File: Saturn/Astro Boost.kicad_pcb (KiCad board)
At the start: 2 copper layers, 59 x 130 mm, 35 parts, among them J1 AudioJack2, J10 Power from SW to PS, J11 +9V, J12 -9V, J2 AudioJack2, J3 Jack-DC, J4 Signal In, J5 Audio In, J6 Processed to SW, J7 Bypass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

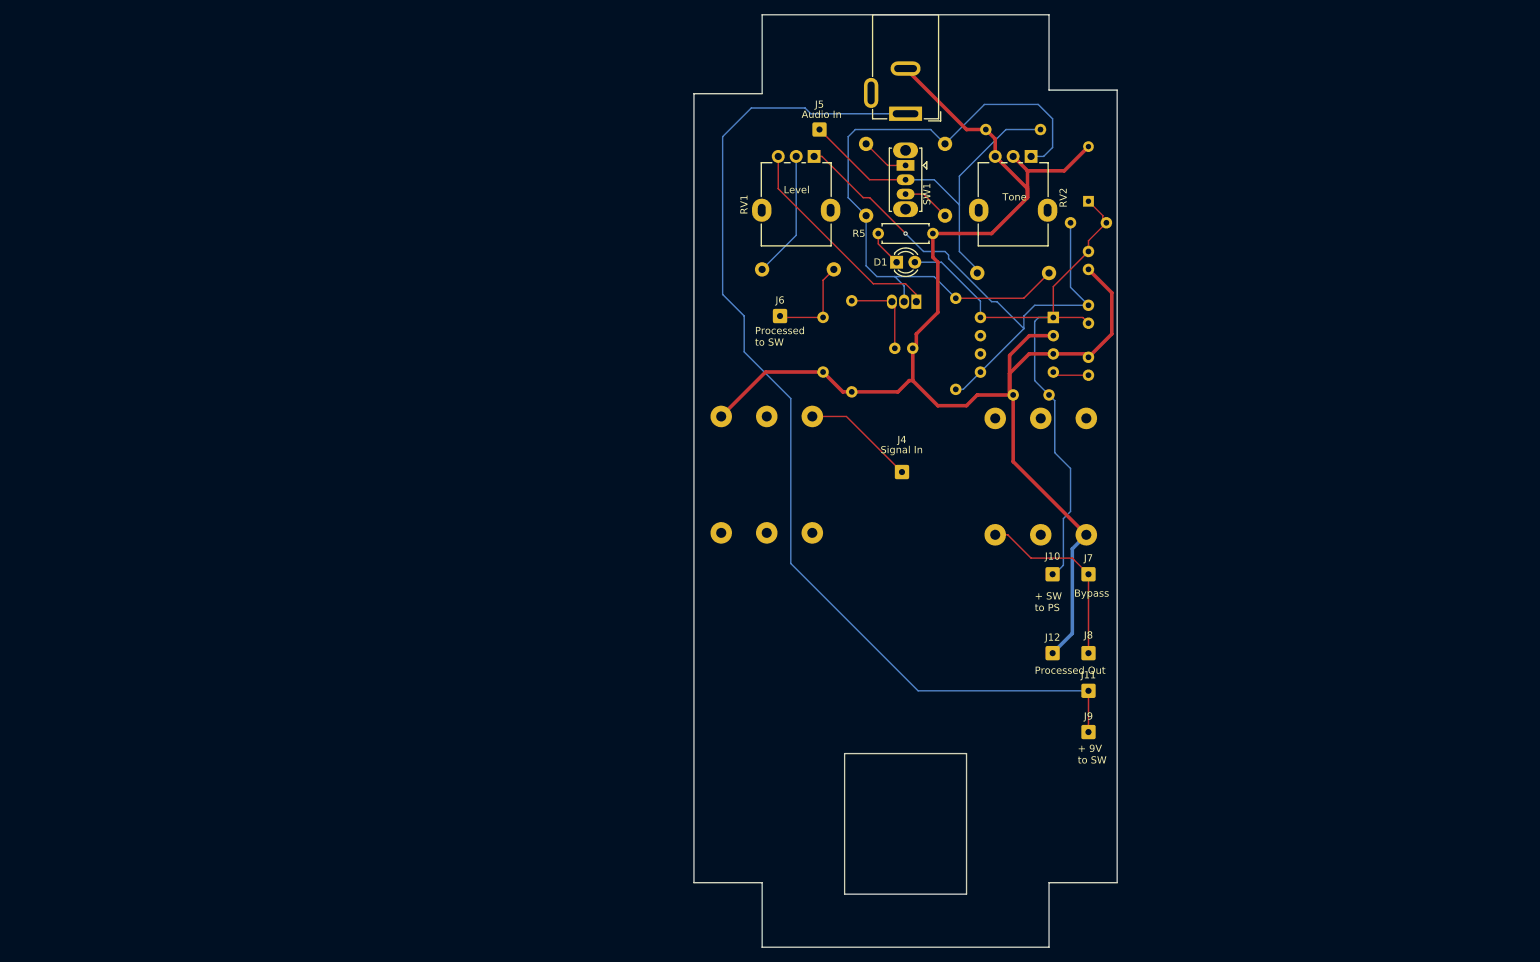
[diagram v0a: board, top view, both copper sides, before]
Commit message: Updates to Saturn
Removed wiring pads and associated tracks
Added to do list
Shortened PCB
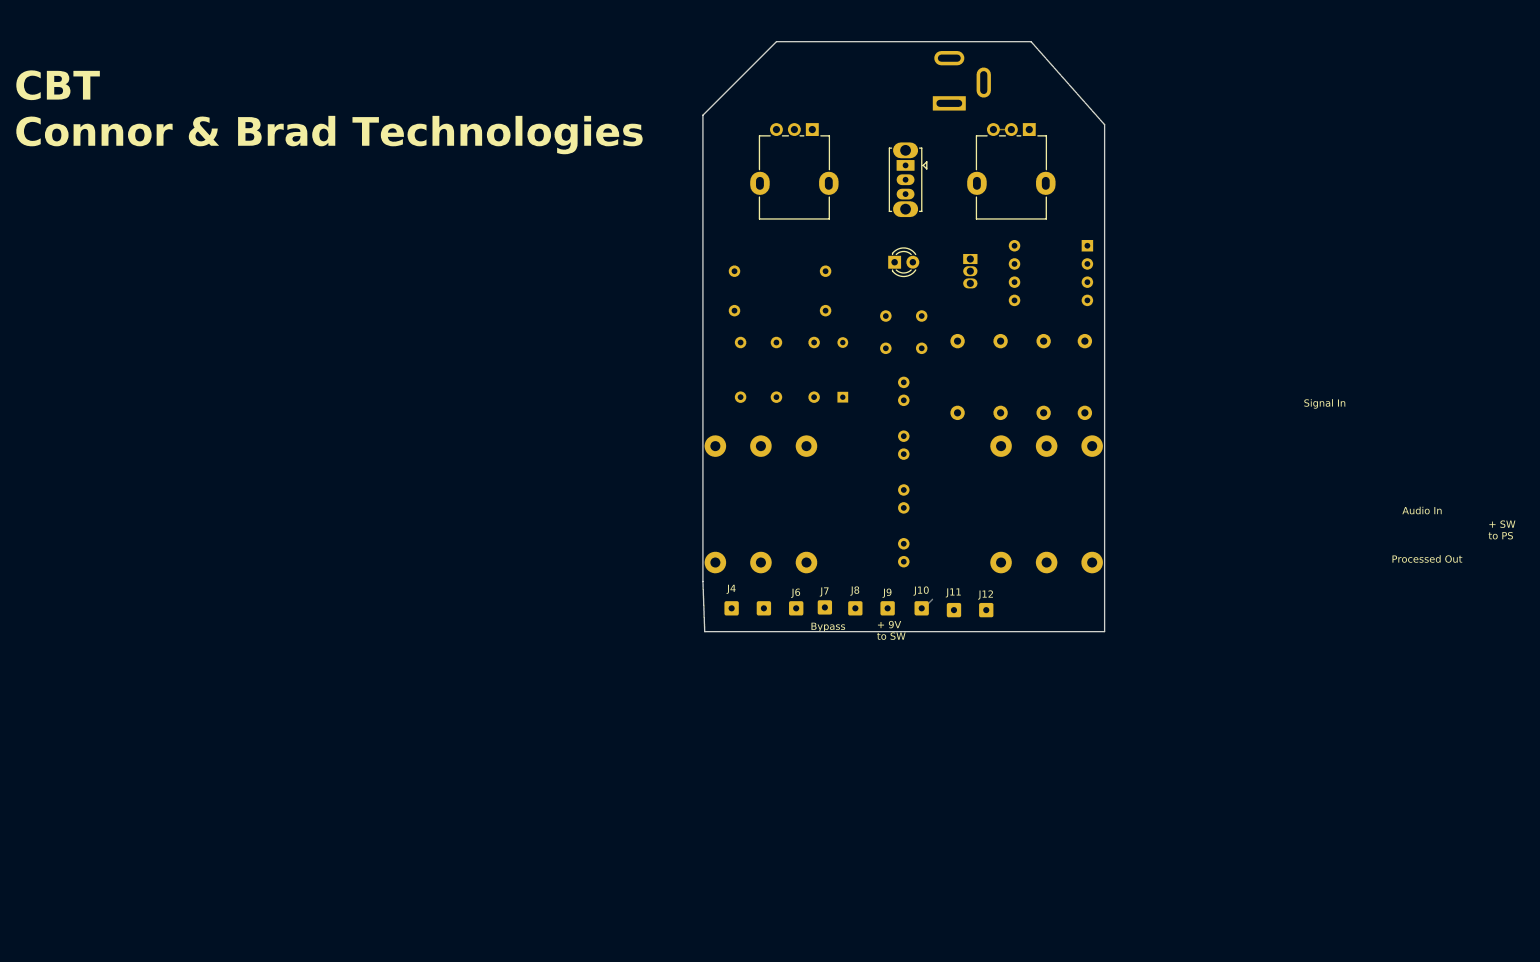
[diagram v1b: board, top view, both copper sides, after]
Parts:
- J3, R5: moved to B.Cu
- moved J5 67.2 mm to (130.8, 104.0)
- moved R4 56.0 mm to (127.5, 74.6), turned to 90 degrees
- moved D2 43.8 mm to (141.8, 74.6)
- moved C5 42.3 mm to (175.5, 76.8), turned to 90 degrees
- moved J6 40.8 mm to (135.2, 104.0)
- moved C8 38.4 mm to (150.2, 97.5), turned to 90 degrees
- moved J7 37.0 mm to (139.2, 103.9)
- moved C4 37.0 mm to (169.8, 76.8)
- moved C6 34.7 mm to (150.2, 87.5), turned to -90 degrees
- moved J8 33.1 mm to (143.5, 104.0)
- moved J9 32.9 mm to (148.0, 104.0)
- moved C9 31.6 mm to (150.2, 72.5)
- moved J4 30.4 mm to (126.2, 104.0)
- moved C7 28.8 mm to (152.8, 63.2)
- moved BT1 27.5 mm to (148.5, 121.8)
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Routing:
- net 0: track 213.2 -> 2.50 mm
- net Power from 9V: track 145.5 -> 0.00 mm
- net Net-(Q1-B): track 92.3 -> 0.00 mm
- net +9V: track 90.7 -> 2.02 mm
- net -9V: track 76.4 -> 0.00 mm, vias 1 -> 0
- net Audio In: track 52.4 -> 0.00 mm
- net Net-(Q1-C): track 30.9 -> 0.00 mm
- net Net-(J7-Pin_1): track 27.0 -> 0.75 mm
- net Net-(C2-Pad2): track 17.7 -> 0.00 mm
- net Net-(J4-Pin_1): track 15.7 -> 0.00 mm
- net Processed to SW: track 13.4 -> 0.27 mm
- net Net-(Q1-E): track 12.3 -> 0.00 mm
- net Net-(SW1-C): track 6.74 -> 0.00 mm
- net Net-(SW1-A): track 6.74 -> 0.00 mm
- net Net-(U1-CAP-): track 5.08 -> 0.00 mm
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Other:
- board size 59 x 130 mm -> 56 x 82.2 mm
- board text added: "CBT Connor & Brad Technologies"
- board text removed: "Level"
- board text removed: "Processed to SW"
- board text removed: "Tone"

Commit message: Saturn PCB Updates
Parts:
- R2, R4, R5: footprint Resistor_THT:R_Axial_DIN0207_L6.3mm_D2.5mm_P7.62mm_Horizontal -> Resistor_THT:R_Axial_DIN0207_L6.3mm_D2.5mm_P10.16mm_Horizontal
- U1: footprint Package_DIP:DIP-8_W10.16mm -> Package_DIP:DIP-8_W7.62mm
- moved D2 14.7 mm to (127.2, 72.8), turned to 0 degrees
- moved R4 12.4 mm to (126.2, 62.2), turned to 0 degrees
- moved R3 4.54 mm to (125.0, 58.2)
- moved R2 4.35 mm to (136.3, 69.0), turned to 180 degrees
- moved R1 3.35 mm to (137.8, 54.0)
- moved R5 2.02 mm to (136.3, 65.5), turned to 180 degrees
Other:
- board text added: "+ -"

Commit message: updates to saturn
layout
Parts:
- moved R4 46.1 mm to (171.2, 52.0), turned to 180 degrees
- moved C4 38.9 mm to (143.5, 48.0)
- moved C5 38.4 mm to (145.5, 52.8), turned to 0 degrees
- moved R1 34.5 mm to (172.2, 56.0)
- moved C1 28.8 mm to (157.5, 38.0)
- moved D2 28.0 mm to (154.1, 80.5), turned to 180 degrees
- moved R2 27.8 mm to (146.5, 94.8), turned to 90 degrees
- moved U1 26.6 mm to (154.1, 68.7)
- moved C8 23.7 mm to (160.2, 76.0)
- moved C3 21.1 mm to (140.5, 63.8)
- moved C2 20.9 mm to (152.8, 84.5)
- moved C6 16.5 mm to (140.8, 74.0)
- moved R3 16.3 mm to (141.2, 56.2), turned to 180 degrees
- moved C9 15.1 mm to (160.2, 61.2)
- moved C10 15.0 mm to (162.8, 68.5), turned to 180 degrees
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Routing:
- net 0: track 2.50 -> 0.00 mm
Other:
- outline, holes or cut-outs redrawn
- board text added: "+"
- board text removed: "+ 9V to SW"
- board text removed: "+ SW to PS"
- board text removed: "Audio In"
- board text removed: "Bypass"
- board text removed: "Processed Out"
- board text removed: "Signal In"

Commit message: Updates to saturn
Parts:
- C1, C5: footprint Capacitor_THT:C_Disc_D9.0mm_W5.0mm_P10.00mm -> Capacitor_THT:C_Axial_L12.0mm_D6.5mm_P20.00mm_Horizontal
- C2, C4: footprint Capacitor_THT:C_Disc_D9.0mm_W5.0mm_P10.00mm -> Capacitor_THT:C_Axial_L12.0mm_D9.5mm_P20.00mm_Horizontal
- J10, J11, J12, J4, J5, J6, J7, J8, J9: moved to B.Cu
- moved C4 42.3 mm to (172.8, 78.5)
- moved J12 35.5 mm to (133.0, 104.0), turned to 180 degrees
- moved J4 35.5 mm to (168.5, 103.8), turned to 180 degrees
- moved C2 35.2 mm to (129.0, 58.5)
- moved J11 26.5 mm to (137.5, 104.0), turned to 180 degrees
- moved J5 26.5 mm to (164.0, 103.8), turned to 180 degrees
- moved C1 24.1 mm to (175.8, 53.8), turned to 180 degrees
- moved C5 20.5 mm to (125.0, 53.8)
- moved J10 17.5 mm to (142.0, 103.8), turned to 180 degrees
- moved J6 17.5 mm to (159.5, 103.8), turned to 180 degrees
- moved R1 17.2 mm to (156.5, 49.1), turned to 90 degrees
- moved R2 11.2 mm to (145.2, 83.8), turned to 0 degrees
- moved R4 10.9 mm to (161.0, 48.1), turned to 90 degrees
- moved J7 9.50 mm to (155.5, 103.6), turned to 180 degrees
- moved J9 8.00 mm to (146.8, 103.8), turned to 180 degrees
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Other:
- outline, holes or cut-outs redrawn
- board text added: "C10"
- board text added: "C2"
- board text added: "C3"
- board text added: "C4"
- board text added: "C6"
- board text added: "C7"
- board text added: "C8"
- board text added: "C9"
- board text added: "D2"
- board text added: "Q1"
- board text added: "R1"
- board text added: "R3"
